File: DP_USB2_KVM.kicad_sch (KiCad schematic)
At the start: 144 parts, among them J1 USB4056-03-A_REVA2, J10 67298-3090, J2 47272-0001, J3 USB_A, J4 USB_A_Recept, J5 Conn_Keyboard_Amiga500, J6 USB_A, J7 CF31401D0R0-05-NH, J8 67298-3090, J9 Conn_QMTECH_Cyclone_V_SoC_KFB, Q1 MMBT3904, Q2 MMBT3904, SW4.KVM1 1-1825027-1, U1 TPS563240DDC, U10 SN75DP120RHHT, U11 CH334R, U12 CH334R, U2 TPS563240DDC, U3 FUSB307BMPX, U4 HD3SS460RHR, U5 CH334R, U6 HD3SS215, U7 CH334R, U8 ESP32-S3-WROOM-2, U9 CH340K, Y1 12MHz, Y2 12MHz, Y3 12MHz, Y4 12MHz

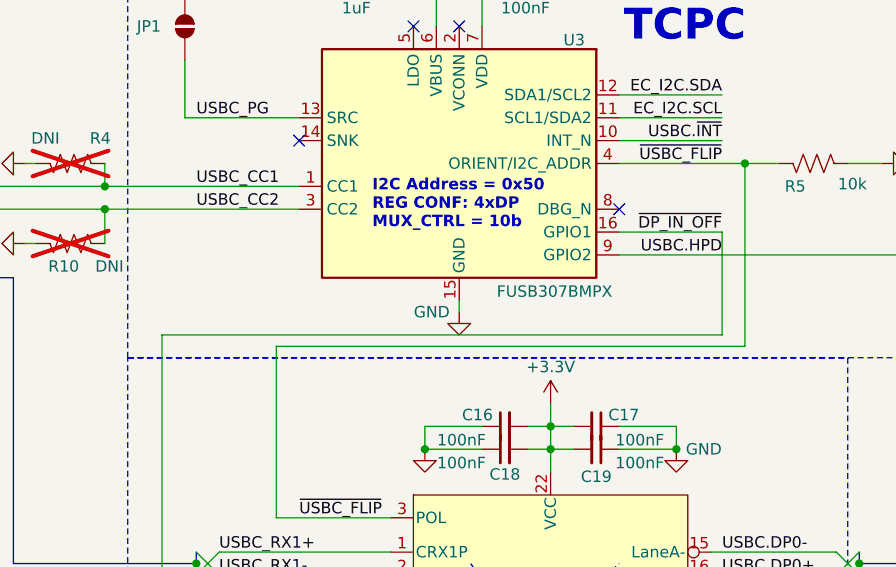
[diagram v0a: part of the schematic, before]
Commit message: BUG Fix: TCPC GPIO nets separated
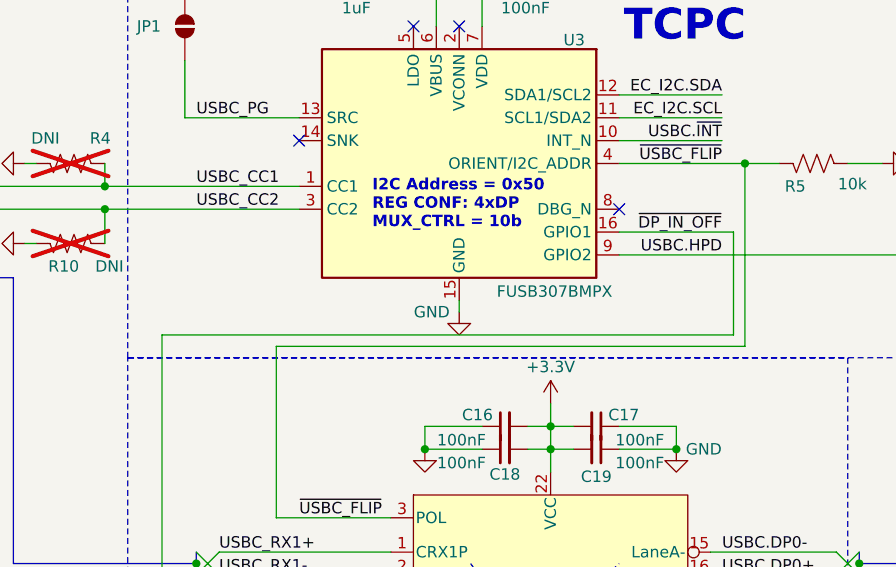
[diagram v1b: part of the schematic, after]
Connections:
- net USBC.HPD: no longer R15.1, U3.16 (GPIO1), U4.17 (EN)
- new net ~{DP_IN_OFF}: R15.1, U3.16 (GPIO1), U4.17 (EN)
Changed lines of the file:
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@@
 	(wire
 		(pts
-			(xy 241.3 55.88) (xy 241.3 67.31)
-		)
-		(stroke
-			(width 0)
-			(type default)
-		)
-	)
-	(wire
-		(pts
 			(xy 116.84 208.28) (xy 120.65 208.28)
 		)
@@
 	(wire
 		(pts
+			(xy 242.57 55.88) (xy 242.57 67.31)
+		)
+		(stroke
+			(width 0)
+			(type default)
+		)
+	)
+	(wire
+		(pts
 			(xy 444.5 182.88) (xy 429.26 182.88)
 		)
@@
 	(wire
 		(pts
-			(xy 179.07 67.31) (xy 241.3 67.31)
+			(xy 179.07 67.31) (xy 242.57 67.31)
 		)
 		(stroke
@@
 	(wire
 		(pts
-			(xy 229.87 55.88) (xy 241.3 55.88)
+			(xy 229.87 55.88) (xy 242.57 55.88)
 		)
 		(stroke
@@
 		)
 		(pin "9"
-			(alternate "IO16")
 		)
 		(pin "15"

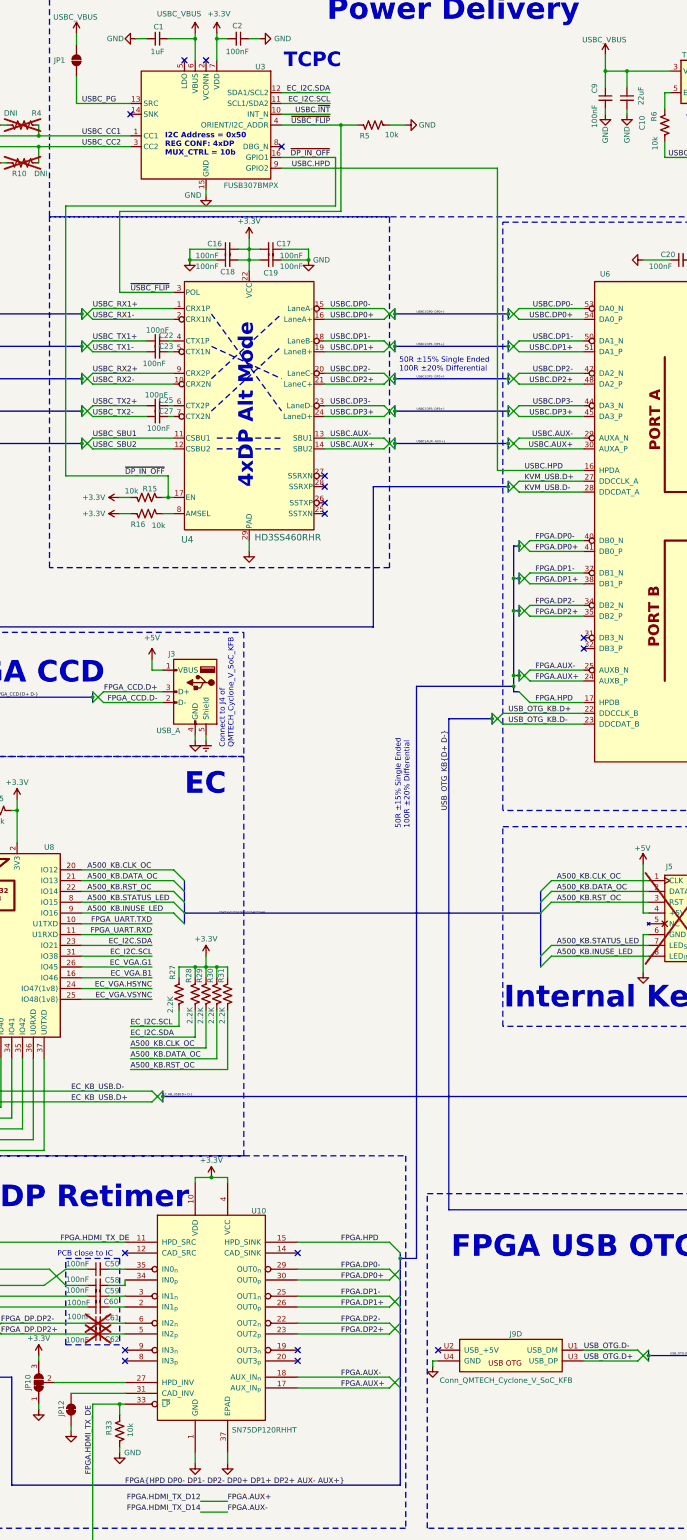
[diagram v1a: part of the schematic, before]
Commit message: BUG Fix: Using TCPC SINK pin as USBC_PG to enable dead battery power-up sequence
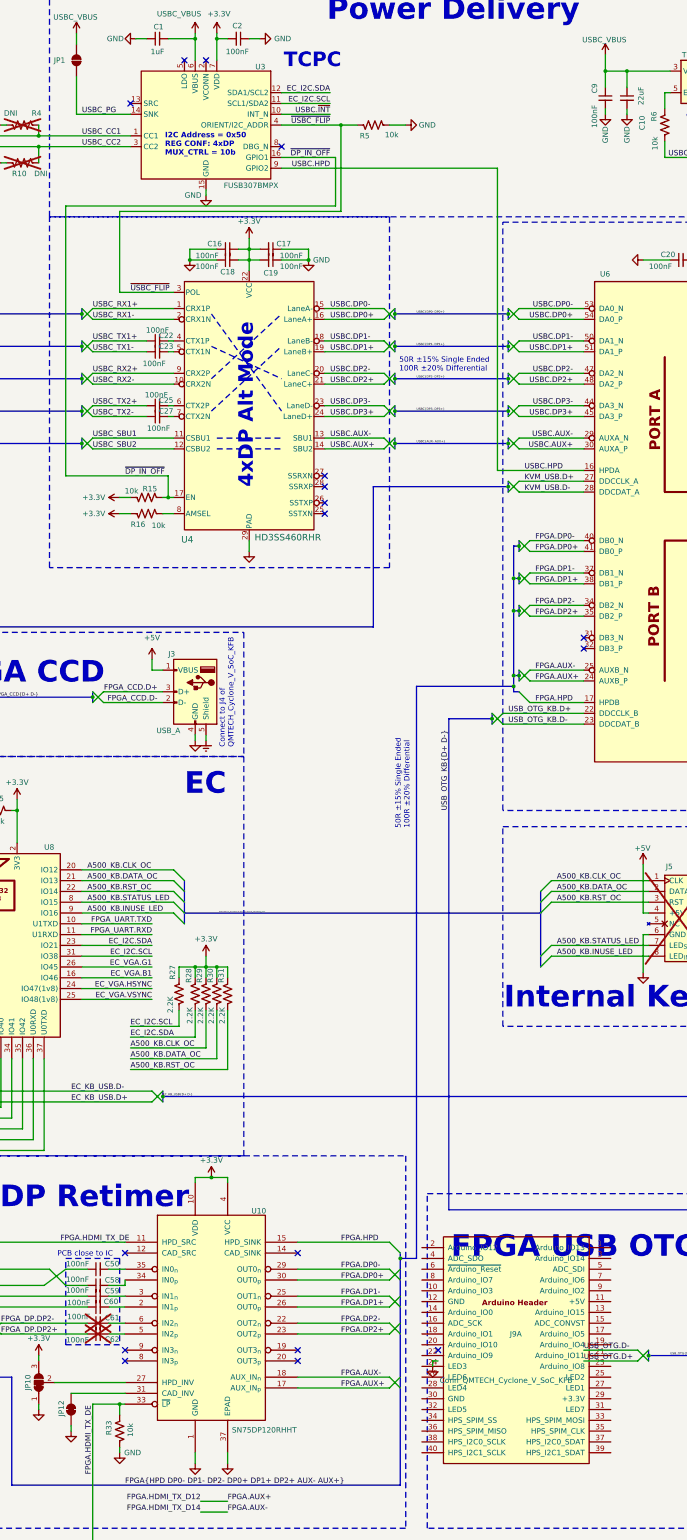
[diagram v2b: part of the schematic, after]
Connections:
- net GND: no longer J9.U4 (GND)
- net USBC_PG: now also U3.14 (SNK); no longer U3.13 (SRC)
- net USB_OTG.D+: no longer J9.U3 (USB_DP)
- net USB_OTG.D-: no longer J9.U1 (USB_DM)

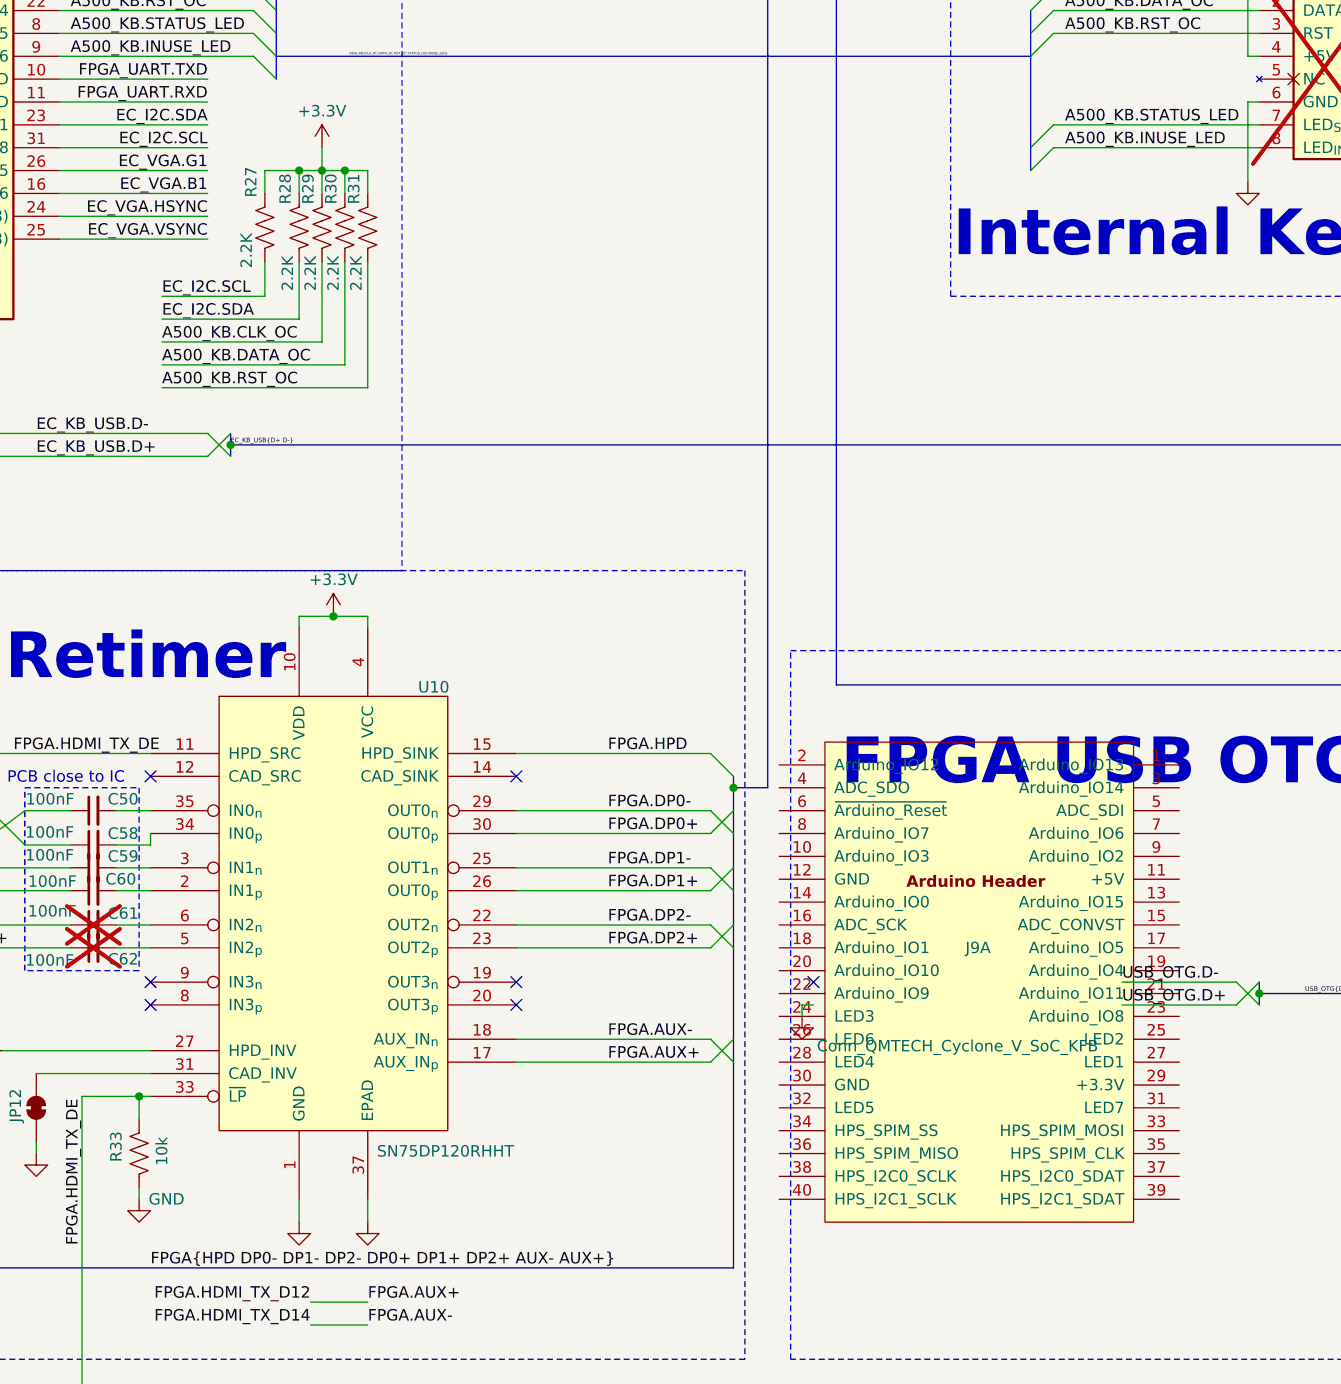
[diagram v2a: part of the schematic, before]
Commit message: BUG Fix: Pull Up resistor on USBC_INT_n
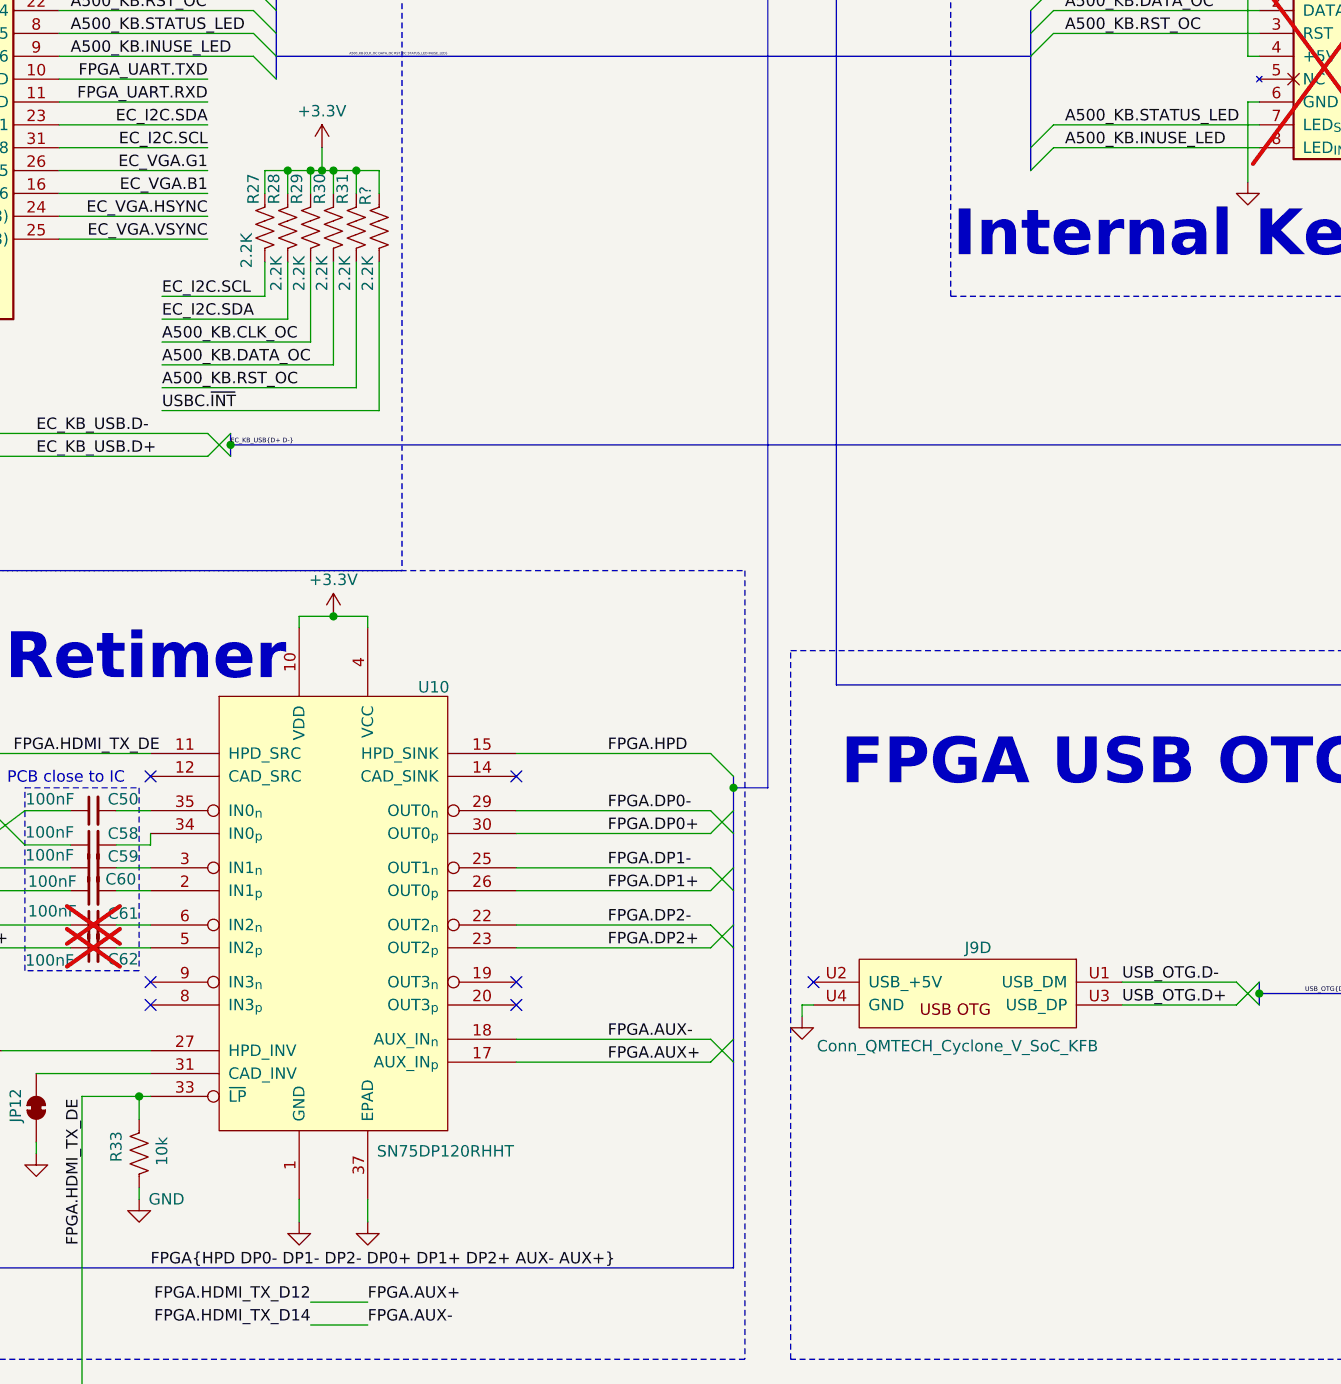
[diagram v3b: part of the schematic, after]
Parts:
- added R31: 2.2K, Resistor_SMD:R_0603_1608Metric_Pad0.98x0.95mm_HandSolder, symbol Device:R_US
- renumbered R31 to R?
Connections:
- net +3.3V: now also R31.2
- net A500_KB.RST_OC: now also R31.1; no longer R?.1
- net GND: now also J9.U4 (GND)
- net USBC.~{INT}: now also R?.1
- net USB_OTG.D+: now also J9.U3 (USB_DP)
- net USB_OTG.D-: now also J9.U1 (USB_DM)
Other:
- moved on the sheet: R28, R29, R30, R?

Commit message: Cleared the annotation and regenerated PDF schematic
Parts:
- renumbered C1 to C?, C11 to C?, C22 to C?, C62 to C?, C4 to C?, C25 to C?, C8 to C?, C35 to C?, C12 to C?, C41 to C?, C14 to C?, C57 to C?, C34 to C?, C36 to C?, C43 to C?, C42 to C?, C37 to C?, C38 to C?, C19 to C?, C44 to C?, C53 to C?, C47 to C?, C17 to C?, C60 to C?, C58 to C?, C49 to C?, C52 to C?, C6 to C?, C61 to C?, C45 to C?, C39 to C?, C50 to C?, C56 to C?, C54 to C?, C20 to C?, C16 to C?, C59 to C?, C13 to C?, C10 to C?, C24 to C?, C32 to C?, C15 to C?, C51 to C?, C33 to C?, C23 to C?, C48 to C?, C9 to C?, C21 to C?, C30 to C?, C40 to C?, C18 to C?, C29 to C?, C2 to C?, C7 to C?, C26 to C?, C28 to C?, C27 to C?, C31 to C?, C5 to C?, C55 to C?, C46 to C?, J5 to J?, J3 to J?, J9 to J?, J6 to J?, J1 to J?, J4 to J?, J7 to J?, J2 to J?, J8 to J?, J10 to J?, JP11 to JP?, JP3 to JP?, JP16 to JP?, JP14 to JP?, JP19 to JP?, JP10 to JP?, JP1 to JP?, JP7 to JP?, JP8 to JP?, JP13 to JP?, JP5 to JP?, JP18 to JP?, JP4 to JP?, JP17 to JP?, JP15 to JP?, JP9 to JP?, JP6 to JP?, JP12 to JP?, JP2 to JP?, L2 to L?, L1 to L?, Q1 to Q?, Q2 to Q?, R24 to R?, R14 to R?, R5 to R?, R12 to R?, R10 to R?, R8 to R?, R22 to R?, R27 to R?, R6 to R?, R7 to R?, R9 to R?, R2 to R?, R4 to R?, R18 to R?, R23 to R?, R33 to R?, R19 to R?, R26 to R?, R20 to R?, R28 to R?, R17 to R?, R30 to R?, R13 to R?, R11 to R?, R21 to R?, R32 to R?, R16 to R?, R3 to R?, R15 to R?, R29 to R?, R31 to R?, R1 to R?, R25 to R?, SW4.KVM1 to SW4.KVM?, U12 to U?, U1 to U?, U7 to U?, U11 to U?, U9 to U?, U3 to U?, U4 to U?, U8 to U?, U6 to U?, U2 to U?, U10 to U?, U5 to U?, Y3 to Y?, Y4 to Y?, Y1 to Y?, Y2 to Y?
